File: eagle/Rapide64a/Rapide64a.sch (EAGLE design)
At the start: 4 parts, among them IC1 MEGA64-A

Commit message: Version 0 before the manual wiring
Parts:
- added C1, C2: 22pF, resistor:C-EU025-024X044
- added H1, H2, H3: MOUNT-HOLE2.8, holes:MOUNT-HOLE2.8
- added J1: AVR_SPI_PRG_6PTH, SparkFun-Connectors:AVR_SPI_PRG_6PTH
- added JP4, JP5, JP6, JP7, JP8, JP_ROW_GND, JP_ROW_VCC: M161X16_NO_SILK, SparkFun-Connectors:M161X16_NO_SILK
- added JP_A_C, JP_E_D: M16PTH, SparkFun-Connectors:M16PTH
- added JP_B, JP_F, JP_G: (no value), SparkFun-Connectors:M081X08
- added JP_POWER: (no value), SparkFun-Connectors:M02LOCK_LONGPADS
- added JP_X: (no value), SparkFun-Connectors:M02PTH
- added Y1: (no value), SparkFun-FreqCtrl:CRYSTALHC49UV
- JP1, JP2, JP3: value M16PTH -> M161X16_NO_SILK; device SparkFun-Connectors:M16PTH -> SparkFun-Connectors:M161X16_NO_SILK
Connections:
- new net GND: C1.1, C2.1, IC1.GND, IC1.GND@1, IC1.GND@2, J1.6, JP_G.7, JP_POWER.1, JP_ROW_GND.1, JP_ROW_GND.10, JP_ROW_GND.11, JP_ROW_GND.12, JP_ROW_GND.13, JP_ROW_GND.14, JP_ROW_GND.15, JP_ROW_GND.16, JP_ROW_GND.2, JP_ROW_GND.3, JP_ROW_GND.4, JP_ROW_GND.5, JP_ROW_GND.6, JP_ROW_GND.7, JP_ROW_GND.8, JP_ROW_GND.9
- new net N$33: IC1.(SS)PB0, JP_B.1
- new net N$34: IC1.(SCK)PB1, J1.3, JP_B.2
- new net N$35: IC1.(MOSI)PB2, J1.4, JP_B.3
- new net N$36: IC1.(MISO)PB3, J1.1, JP_B.4
- new net N$37: IC1.(OC0)PB4, JP_B.5
- new net N$38: IC1.(OC1A)PB5, JP_B.6
- new net N$39: IC1.(OC1B)PB6, JP_B.7
- new net N$40: IC1.(OC2/OC1C)PB7, JP_B.8
- new net N$41: IC1.PF0(ADC0), JP_F.1
- new net N$42: IC1.PF1(ADC1), JP_F.2
- new net N$43: IC1.PF2(ADC2), JP_F.3
- new net N$44: IC1.PF3(ADC3), JP_F.4
- new net N$45: IC1.PF4(ADC4/TCK), JP_F.5
- new net N$46: IC1.PF5(ADC5/TMS), JP_F.6
- new net N$47: IC1.PF6(ADC6/TDO), JP_F.7
- new net N$48: IC1.PF7(ADC7/TDI), JP_F.8
- new net N$49: IC1.PEN, JP_G.1
- new net N$50: IC1.PG0(WR), JP_G.2
- new net N$51: IC1.PG1(RD), JP_G.3
- new net N$52: IC1.PG2(ALE), JP_G.4
- new net N$53: IC1.PG4(TOSC1), JP_G.5
- new net N$54: IC1.PG3(TOSC2), JP_G.6
- new net N$57: IC1.RESET, J1.5, JP_X.2
- new net N$58: IC1.AREF, JP_X.1
- new net N$59: C1.2, IC1.XTAL2, Y1.2
- new net N$60: C2.2, IC1.XTAL1, Y1.1
- new net VCC: IC1.AVCC, IC1.VCC, IC1.VCC@1, J1.2, JP_G.8, JP_POWER.2, JP_ROW_VCC.1, JP_ROW_VCC.10, JP_ROW_VCC.11, JP_ROW_VCC.12, JP_ROW_VCC.13, JP_ROW_VCC.14, JP_ROW_VCC.15, JP_ROW_VCC.16, JP_ROW_VCC.2, JP_ROW_VCC.3, JP_ROW_VCC.4, JP_ROW_VCC.5, JP_ROW_VCC.6, JP_ROW_VCC.7, JP_ROW_VCC.8, JP_ROW_VCC.9
- net N$1: now also JP_E_D.1; no longer JP3.1
- net N$10: now also IC1.(SDA/INT1)PD1, JP_E_D.10; no longer IC1.(SCK)PB1, JP3.10
- net N$11: now also IC1.(RXD1/INT2)PD2, JP_E_D.11; no longer IC1.(MOSI)PB2, JP3.11
- net N$12: now also IC1.(TXD1/INT3)PD3, JP_E_D.12; no longer IC1.(MISO)PB3, JP3.12
- net N$13: now also IC1.(IC1)PD4, JP_E_D.13; no longer IC1.(OC0)PB4, JP3.13
- net N$14: now also IC1.(XCK1)PD5, JP_E_D.14; no longer IC1.(OC1A)PB5, JP3.14
- net N$15: now also IC1.(T1)PD6, JP_E_D.15; no longer IC1.(OC1B)PB6, JP3.15
- net N$16: now also IC1.(T2)PD7, JP_E_D.16; no longer IC1.(OC2/OC1C)PB7, JP3.16
- net N$17: now also JP_A_C.1; no longer JP1.1
- net N$18: now also JP_A_C.2; no longer JP1.2
- net N$19: now also JP_A_C.3; no longer JP1.3
- net N$2: now also JP_E_D.2; no longer JP3.2
- net N$20: now also JP_A_C.4; no longer JP1.4
- net N$21: now also JP_A_C.5; no longer JP1.5
- net N$22: now also JP_A_C.6; no longer JP1.6
- net N$23: now also JP_A_C.7; no longer JP1.7
- net N$24: now also JP_A_C.8; no longer JP1.8
- net N$25: now also JP_A_C.9; no longer JP1.9
- net N$26: now also JP_A_C.10; no longer JP1.10
- net N$27: now also JP_A_C.11; no longer JP1.11
- net N$28: now also JP_A_C.12; no longer JP1.12
- net N$29: now also JP_A_C.13; no longer JP1.13
- net N$3: now also JP_E_D.3; no longer JP3.3
- net N$30: now also JP_A_C.14; no longer JP1.14
- net N$31: now also JP_A_C.15; no longer JP1.15
- net N$32: now also JP_A_C.16; no longer JP1.16
- net N$4: now also JP_E_D.4; no longer JP3.4
- net N$5: now also JP_E_D.5; no longer JP3.5
- net N$6: now also JP_E_D.6; no longer JP3.6
- net N$7: now also JP_E_D.7; no longer JP3.7
- net N$8: now also JP_E_D.8; no longer JP3.8
- net N$9: now also IC1.(SCL/INT0)PD0, JP_E_D.9; no longer IC1.(SS)PB0, JP3.9
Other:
- moved on the sheet: JP1, JP2, JP3

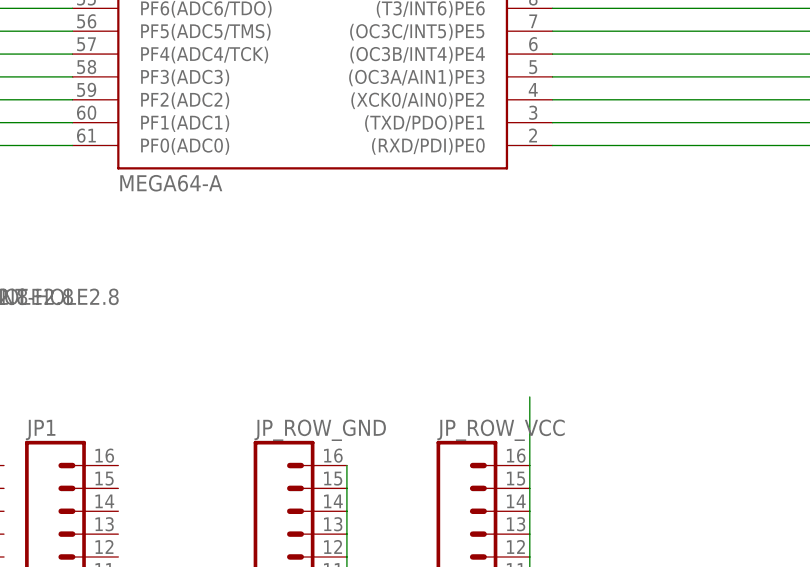
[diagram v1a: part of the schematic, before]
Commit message: Added 2 pushbuttons
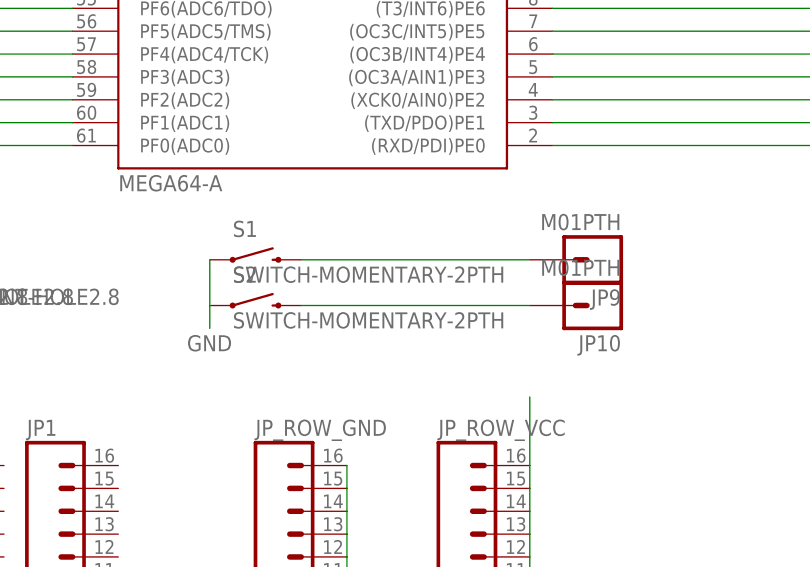
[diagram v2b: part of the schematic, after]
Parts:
- added JP10, JP9: M01PTH, SparkFun-Connectors:M01PTH
- added S1, S2: SWITCH-MOMENTARY-2PTH, SparkFun-Electromechanical:SWITCH-MOMENTARY-2PTH
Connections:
- new net N$55: JP9.1, S1.2
- new net N$56: JP10.1, S2.2
- net GND: now also S1.1, S2.1
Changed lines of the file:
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@@
 <part name="H3" library="holes" deviceset="MOUNT-HOLE" device="2.8"/>
 <part name="JP8" library="SparkFun-Connectors" deviceset="M16" device="1X16_NO_SILK"/>
+<part name="S1" library="SparkFun-Electromechanical" deviceset="SWITCH-MOMENTARY-2" device="PTH"/>
+<part name="S2" library="SparkFun-Electromechanical" deviceset="SWITCH-MOMENTARY-2" device="PTH"/>
+<part name="JP9" library="SparkFun-Connectors" deviceset="M01" device="PTH"/>
+<part name="JP10" library="SparkFun-Connectors" deviceset="M01" device="PTH"/>
 </parts>
 <sheets>
@@
 <instance part="H3" gate="G$1" x="5.08" y="-7.62"/>
 <instance part="JP8" gate="G$1" x="-53.34" y="-93.98"/>
+<instance part="S1" gate="G$1" x="40.64" y="-5.08"/>
+<instance part="S2" gate="G$1" x="40.64" y="-10.16"/>
+<instance part="JP9" gate="G$1" x="78.74" y="-5.08" rot="R180"/>
+<instance part="JP10" gate="G$1" x="78.74" y="-10.16" rot="R180"/>
 </instances>
 <busses>
@@
 <label x="50.8" y="-78.74" size="1.778" layer="95"/>
 </segment>
-</net>
+<segment>
+<pinref part="S1" gate="G$1" pin="1"/>
+<pinref part="S2" gate="G$1" pin="1"/>
+<wire x1="35.56" y1="-5.08" x2="35.56" y2="-10.16" width="0.1524" layer="91"/>
+<wire x1="35.56" y1="-10.16" x2="35.56" y2="-12.7" width="0.1524" layer="91"/>
+<label x="33.02" y="-15.24" size="1.778" layer="95"/>
+</segment>
+</net>
+<net name="N$55" class="0">
+<segment>
+<pinref part="S1" gate="G$1" pin="2"/>
+<pinref part="JP9" gate="G$1" pin="1"/>
+<wire x1="45.72" y1="-5.08" x2="71.12" y2="-5.08" width="0.1524" layer="91"/>
+</segment>
+</net>
+<net name="N$56" class="0">
+<segment>
+<pinref part="S2" gate="G$1" pin="2"/>
+<pinref part="JP10" gate="G$1" pin="1"/>
+<wire x1="45.72" y1="-10.16" x2="71.12" y2="-10.16" width="0.1524" layer="91"/>
+</segment>
+</net>

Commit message: Work in progress, 40% wiring done.
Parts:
- JP_POWER: device SparkFun-Connectors:M02LOCK_LONGPADS -> SparkFun-Connectors:M02PTH
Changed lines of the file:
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@@
 <part name="C2" library="resistor" deviceset="C-EU" device="025-024X044" value="22pF"/>
 <part name="Y1" library="SparkFun-FreqCtrl" deviceset="CRYSTAL" device="HC49UV"/>
-<part name="JP_POWER" library="SparkFun-Connectors" deviceset="M02" device="LOCK_LONGPADS"/>
+<part name="JP_POWER" library="SparkFun-Connectors" deviceset="M02" device="PTH"/>
 <part name="J1" library="SparkFun-Connectors" deviceset="AVR_SPI_PRG_6" device="PTH"/>
 <part name="JP_ROW_VCC" library="SparkFun-Connectors" deviceset="M16" device="1X16_NO_SILK"/>
@@
 </segment>
 </net>
-<net name="N$2" class="0">
+<net name="N$61" class="0">
 <segment>
 <pinref part="IC1" gate="G$1" pin="(TXD/PDO)PE1"/>
@@
 </segment>
 </net>
-<net name="N$3" class="0">
+<net name="N$62" class="0">
 <segment>
 <pinref part="IC1" gate="G$1" pin="(XCK0/AIN0)PE2"/>
@@
 </segment>
 </net>
-<net name="N$4" class="0">
+<net name="N$63" class="0">
 <segment>
 <pinref part="IC1" gate="G$1" pin="(OC3A/AIN1)PE3"/>
@@
 </segment>
 </net>
-<net name="N$5" class="0">
+<net name="N$2" class="0">
 <segment>
 <pinref part="IC1" gate="G$1" pin="(OC3B/INT4)PE4"/>
@@
 </segment>
 </net>
-<net name="N$6" class="0">
+<net name="N$3" class="0">
 <segment>
 <pinref part="IC1" gate="G$1" pin="(OC3C/INT5)PE5"/>
@@
 </segment>
 </net>
-<net name="N$7" class="0">
+<net name="N$4" class="0">
 <segment>
 <pinref part="IC1" gate="G$1" pin="(T3/INT6)PE6"/>
@@
 </segment>
 </net>
-<net name="N$8" class="0">
+<net name="N$6" class="0">
 <segment>
 <pinref part="IC1" gate="G$1" pin="(IC3/INT7)PE7"/>
@@
 </segment>
 </net>
-<net name="N$9" class="0">
+<net name="N$5" class="0">
 <segment>
 <pinref part="JP_E_D" gate="G$1" pin="9"/>
@@
 </segment>
 </net>
-<net name="N$10" class="0">
+<net name="N$7" class="0">
 <segment>
 <pinref part="JP_E_D" gate="G$1" pin="10"/>
@@
 </segment>
 </net>
-<net name="N$11" class="0">
+<net name="N$8" class="0">
 <segment>
 <pinref part="JP_E_D" gate="G$1" pin="11"/>
@@
 </segment>
 </net>
-<net name="N$12" class="0">
+<net name="N$64" class="0">
 <segment>
 <pinref part="JP_E_D" gate="G$1" pin="12"/>
@@
 </segment>
 </net>
-<net name="N$13" class="0">
+<net name="N$65" class="0">
 <segment>
 <pinref part="JP_E_D" gate="G$1" pin="13"/>
@@
 </segment>
 </net>
-<net name="N$14" class="0">
+<net name="N$66" class="0">
 <segment>
 <pinref part="JP_E_D" gate="G$1" pin="14"/>
@@
 </segment>
 </net>
-<net name="N$15" class="0">
+<net name="N$67" class="0">
 <segment>
 <pinref part="JP_E_D" gate="G$1" pin="15"/>
@@
 </segment>
 </net>
-<net name="N$16" class="0">
+<net name="N$68" class="0">
 <segment>
 <pinref part="JP_E_D" gate="G$1" pin="16"/>
@@
 </segment>
 </net>
-<net name="N$17" class="0">
+<net name="N$43" class="0">
 <segment>
 <pinref part="IC1" gate="G$1" pin="(AD0)PA0"/>
@@
 </segment>
 </net>
-<net name="N$18" class="0">
+<net name="N$44" class="0">
 <segment>
 <pinref part="IC1" gate="G$1" pin="(AD1)PA1"/>
@@
 </segment>
 </net>
-<net name="N$19" class="0">
+<net name="N$17" class="0">
 <segment>
 <pinref part="IC1" gate="G$1" pin="(AD2)PA2"/>
@@
 </segment>
 </net>
-<net name="N$41" class="0">
+<net name="N$70" class="0">
 <segment>
 <pinref part="JP_F" gate="G$1" pin="1"/>
@@
 </segment>
 </net>
-<net name="N$42" class="0">
+<net name="N$71" class="0">
 <segment>
 <pinref part="JP_F" gate="G$1" pin="2"/>
@@
 </segment>
 </net>
-<net name="N$43" class="0">
+<net name="N$72" class="0">
 <segment>
 <pinref part="JP_F" gate="G$1" pin="3"/>
@@
 </segment>
 </net>
-<net name="N$44" class="0">
+<net name="N$9" class="0">
 <segment>
 <pinref part="JP_F" gate="G$1" pin="4"/>
@@
 </segment>
 </net>
-<net name="N$45" class="0">
+<net name="N$10" class="0">
 <segment>
 <pinref part="JP_F" gate="G$1" pin="5"/>
@@
 </segment>
 </net>
-<net name="N$46" class="0">
+<net name="N$11" class="0">
 <segment>
 <pinref part="JP_F" gate="G$1" pin="6"/>
@@
 </segment>
 </net>
-<net name="N$47" class="0">
+<net name="N$12" class="0">
 <segment>
 <pinref part="JP_F" gate="G$1" pin="7"/>
@@
 </segment>
 </net>
-<net name="N$48" class="0">
+<net name="N$13" class="0">
 <segment>
 <pinref part="JP_F" gate="G$1" pin="8"/>
@@
 </segment>
 </net>
-<net name="N$55" class="0">
+<net name="N$41" class="0">
 <segment>
 <pinref part="S1" gate="G$1" pin="2"/>
@@
 </segment>
 </net>
-<net name="N$56" class="0">
+<net name="N$46" class="0">
 <segment>
 <pinref part="S2" gate="G$1" pin="2"/>

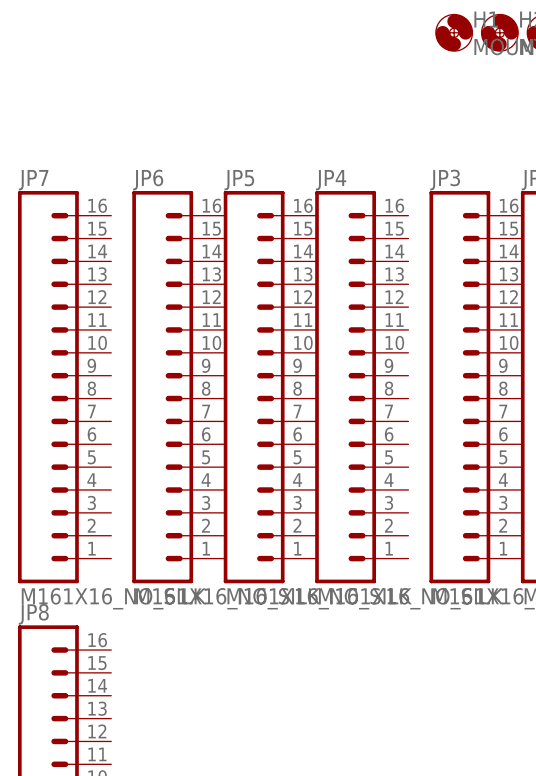
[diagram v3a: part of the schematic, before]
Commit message: Work in progress, changed layout a little, 60% wiring
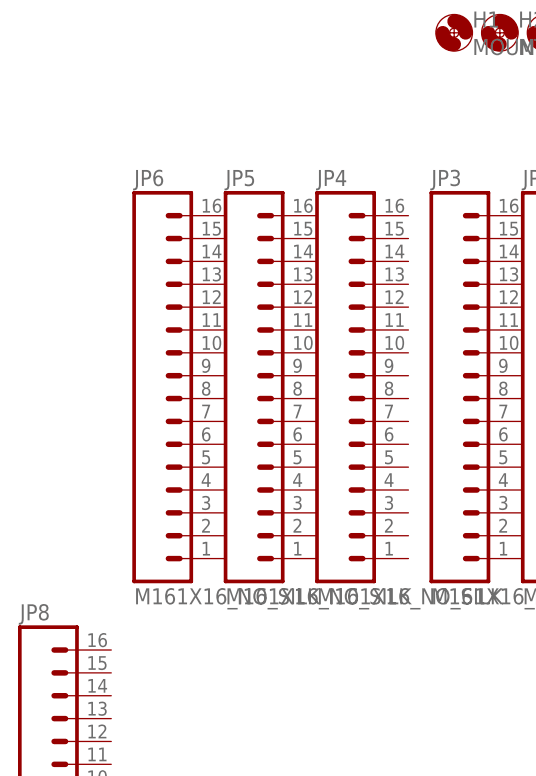
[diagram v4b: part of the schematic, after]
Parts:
- removed JP7: M161X16_NO_SILK, SparkFun-Connectors:M161X16_NO_SILK
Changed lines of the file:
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@@
 <part name="JP5" library="SparkFun-Connectors" deviceset="M16" device="1X16_NO_SILK"/>
 <part name="JP6" library="SparkFun-Connectors" deviceset="M16" device="1X16_NO_SILK"/>
-<part name="JP7" library="SparkFun-Connectors" deviceset="M16" device="1X16_NO_SILK"/>
 <part name="H1" library="holes" deviceset="MOUNT-HOLE" device="2.8"/>
 <part name="H2" library="holes" deviceset="MOUNT-HOLE" device="2.8"/>
@@
 <instance part="JP5" gate="G$1" x="-30.48" y="-45.72"/>
 <instance part="JP6" gate="G$1" x="-40.64" y="-45.72"/>
-<instance part="JP7" gate="G$1" x="-53.34" y="-45.72"/>
 <instance part="H1" gate="G$1" x="-5.08" y="-7.62"/>
 <instance part="H2" gate="G$1" x="0" y="-7.62"/>
@@
 </segment>
 </net>
-<net name="N$33" class="0">
+<net name="N$16" class="0">
 <segment>
 <pinref part="IC1" gate="G$1" pin="(SS)PB0"/>
@@
 </segment>
 </net>
-<net name="N$34" class="0">
+<net name="N$15" class="0">
 <segment>
 <pinref part="IC1" gate="G$1" pin="(SCK)PB1"/>
@@
 </segment>
 </net>
-<net name="N$37" class="0">
+<net name="N$42" class="0">
 <segment>
 <pinref part="IC1" gate="G$1" pin="(OC0)PB4"/>
@@
 </segment>
 </net>
-<net name="N$38" class="0">
+<net name="N$45" class="0">
 <segment>
 <pinref part="IC1" gate="G$1" pin="(OC1A)PB5"/>
@@
 </segment>
 </net>
-<net name="N$39" class="0">
+<net name="N$48" class="0">
 <segment>
 <pinref part="IC1" gate="G$1" pin="(OC1B)PB6"/>
@@
 </segment>
 </net>
-<net name="N$40" class="0">
+<net name="N$18" class="0">
 <segment>
 <pinref part="IC1" gate="G$1" pin="(OC2/OC1C)PB7"/>

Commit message: Wiring finished, must be validated and improved now.
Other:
- moved on the sheet: JP8
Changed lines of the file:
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@@
 <instance part="H2" gate="G$1" x="0" y="-7.62"/>
 <instance part="H3" gate="G$1" x="5.08" y="-7.62"/>
-<instance part="JP8" gate="G$1" x="-53.34" y="-93.98"/>
+<instance part="JP8" gate="G$1" x="-53.34" y="-45.72"/>
 <instance part="S1" gate="G$1" x="40.64" y="-5.08"/>
 <instance part="S2" gate="G$1" x="40.64" y="-10.16"/>
@@
 </segment>
 </net>
-<net name="N$20" class="0">
+<net name="N$14" class="0">
 <segment>
 <pinref part="IC1" gate="G$1" pin="(AD3)PA3"/>
@@
 </segment>
 </net>
-<net name="N$21" class="0">
+<net name="N$38" class="0">
 <segment>
 <pinref part="IC1" gate="G$1" pin="(AD4)PA4"/>
@@
 </segment>
 </net>
-<net name="N$22" class="0">
+<net name="N$39" class="0">
 <segment>
 <pinref part="IC1" gate="G$1" pin="(AD5)PA5"/>
@@
 </segment>
 </net>
-<net name="N$23" class="0">
+<net name="N$40" class="0">
 <segment>
 <pinref part="IC1" gate="G$1" pin="(AD6)PA6"/>
@@
 </segment>
 </net>
-<net name="N$24" class="0">
+<net name="N$47" class="0">
 <segment>
 <pinref part="IC1" gate="G$1" pin="(AD7)PA7"/>
@@
 </segment>
 </net>
-<net name="N$25" class="0">
+<net name="N$56" class="0">
 <segment>
 <pinref part="IC1" gate="G$1" pin="(A8)PC0"/>
@@
 </segment>
 </net>
-<net name="N$26" class="0">
+<net name="N$75" class="0">
 <segment>
 <pinref part="IC1" gate="G$1" pin="(A9)PC1"/>
@@
 </segment>
 </net>
-<net name="N$27" class="0">
+<net name="N$73" class="0">
 <segment>
 <pinref part="IC1" gate="G$1" pin="(A10)PC2"/>
@@
 </segment>
 </net>
-<net name="N$28" class="0">
+<net name="N$69" class="0">
 <segment>
 <pinref part="IC1" gate="G$1" pin="(A11)PC3"/>
@@
 </segment>
 </net>
-<net name="N$29" class="0">
+<net name="N$24" class="0">
 <segment>
 <pinref part="IC1" gate="G$1" pin="(A12)PC4"/>
@@
 </segment>
 </net>
-<net name="N$30" class="0">
+<net name="N$51" class="0">
 <segment>
 <pinref part="IC1" gate="G$1" pin="(A13)PC5"/>
@@
 </segment>
 </net>
-<net name="N$31" class="0">
+<net name="N$50" class="0">
 <segment>
 <pinref part="IC1" gate="G$1" pin="(A14)PC6"/>
@@
 </segment>
 </net>
-<net name="N$32" class="0">
+<net name="N$49" class="0">
 <segment>
 <wire x1="129.54" y1="71.12" x2="129.54" y2="137.16" width="0.1524" layer="91"/>
@@
 </segment>
 </net>
-<net name="N$49" class="0">
+<net name="N$19" class="0">
 <segment>
 <pinref part="JP_G" gate="G$1" pin="1"/>
@@
 </segment>
 </net>
-<net name="N$50" class="0">
+<net name="N$20" class="0">
 <segment>
 <pinref part="JP_G" gate="G$1" pin="2"/>
@@
 </segment>
 </net>
-<net name="N$51" class="0">
+<net name="N$21" class="0">
 <segment>
 <pinref part="JP_G" gate="G$1" pin="3"/>
@@
 </segment>
 </net>
-<net name="N$52" class="0">
+<net name="N$37" class="0">
 <segment>
 <pinref part="JP_G" gate="G$1" pin="4"/>
@@
 </segment>
 </net>
-<net name="N$53" class="0">
+<net name="N$23" class="0">
 <segment>
 <pinref part="JP_G" gate="G$1" pin="5"/>
@@
 </segment>
 </net>
-<net name="N$54" class="0">
+<net name="N$22" class="0">
 <segment>
 <pinref part="JP_G" gate="G$1" pin="6"/>
